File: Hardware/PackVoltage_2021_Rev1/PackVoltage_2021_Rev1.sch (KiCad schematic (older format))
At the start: 20 parts

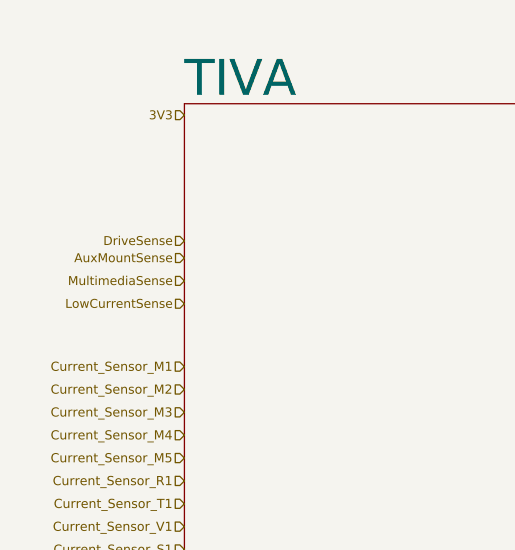
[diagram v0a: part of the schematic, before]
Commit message: Fixed anderson connections
Mistake made when rearranging busses so they would fit on sheet fixed
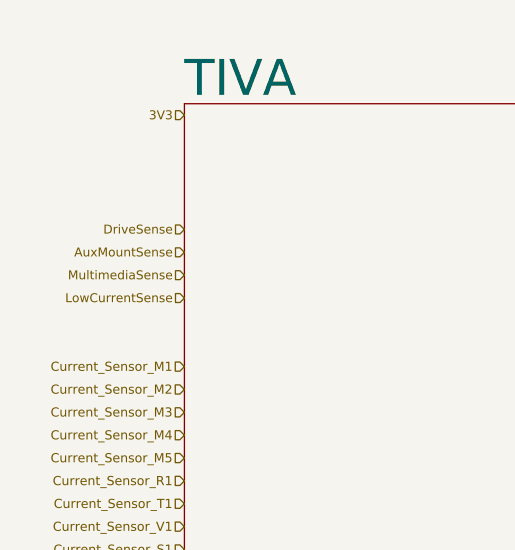
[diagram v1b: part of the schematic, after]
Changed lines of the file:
@@
 Pack Voltage Board
-$Sheet
-S 1200 850  2650 2100
-U 5F74F238
-F0 "TIVA" 157
-F1 "TIVA.sch" 157
-$EndSheet
 $Sheet
 S 1050 3550 2350 1550
@@
 Text Notes 5025 2600 2    79   ~ 0
 PV Tiva Pins
-Text HLabel 1200 1525 0    39   Input ~ 0
+Text HLabel 1200 1500 0    39   Input ~ 0
 AuxMountSense
-Text HLabel 1200 1625 0    39   Input ~ 0
+Text HLabel 1200 1600 0    39   Input ~ 0
 MultimediaSense
-Text HLabel 1200 1725 0    39   Input ~ 0
+Text HLabel 1200 1700 0    39   Input ~ 0
 LowCurrentSense
-Text HLabel 1200 1450 0    39   Input ~ 0
+Text HLabel 1200 1400 0    39   Input ~ 0
 DriveSense
 Wire Notes Line
@@
 	6075 1950 6200 1950
 NoConn ~ 6200 1550
+$Sheet
+S 1200 850  2650 2100
+U 5F74F238
+F0 "TIVA" 157
+F1 "TIVA.sch" 157
+$EndSheet
 $EndSCHEMATC

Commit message: updated busses, fuses, and some names
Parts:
- gave numbers to parts that had none: 1
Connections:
- net Anderson_M5 is gone; now on net Anderson_S1: Conn11.4 (PV+)
- net Anderson_S1: no longer Conn8.4 (PV+)
- new net Anderson_D1: Conn8.4 (PV+)
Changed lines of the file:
@@
 Driver_M3
 Text HLabel 1200 2800 0    40   Input ~ 0
-Current_Sensor_S1
+Current_Sensor_D1
 Text HLabel 1200 2600 0    40   Input ~ 0
 Current_Sensor_T1
@@
 Current_Sensor_V1
 Text HLabel 3850 2800 2    40   Output ~ 0
-Driver_S1
+Driver_D1
 Text HLabel 3850 2600 2    40   Output ~ 0
 Driver_T1
@@
 3V3
 Text HLabel 1050 6900 0    50   Input ~ 0
-Driver_S1
+Driver_D1
 Text HLabel 1050 6800 0    50   Input ~ 0
 Driver_T1
@@
 Current_Sensor_R1
 Text HLabel 3400 6900 2    50   Output ~ 0
-Current_Sensor_S1
+Current_Sensor_D1
 Text HLabel 3400 6800 2    50   Output ~ 0
 Current_Sensor_T1
@@
 Anderson_V1
 Text HLabel 8550 5750 2    50   Input ~ 0
-Anderson_S1
+Anderson_D1
 Text HLabel 3400 3600 2    50   Output ~ 0
 Anderson_M1
@@
 Anderson_V1
 Text HLabel 3400 6050 2    50   Output ~ 0
-Anderson_S1
+Anderson_D1
 Text HLabel 1050 3600 0    50   Input ~ 0
 PV
@@
 	9700 4600 9550 4600
 Text HLabel 9700 4600 2    50   Input ~ 0
-Anderson_M5
+Anderson_S1
 Text HLabel 1050 5050 0    50   Input ~ 0
-Driver_M5
+Driver_S1
 Text HLabel 3400 5050 2    50   Output ~ 0
-Current_Sensor_M5
+Current_Sensor_S1
 Text HLabel 3400 4000 2    50   Output ~ 0
-Anderson_M5
+Anderson_S1
 Text HLabel 1200 2400 0    40   Input ~ 0
-Current_Sensor_M5
+Current_Sensor_S1
 Text HLabel 3850 2400 2    40   Output ~ 0
-Driver_M5
+Driver_S1
 Text HLabel 6075 1850 0    50   Input ~ 0
 CameraCTL
@@
 Driver_A1
 $Comp
-L MRDT_Connectors:Molex_SL_10 Conn?
+L MRDT_Connectors:Molex_SL_10 Conn1
 U 1 1 5F87D729
 P 6400 2100
-F 0 "Conn?" H 6528 2658 60  0000 L CNN
+F 0 "Conn1" H 6528 2658 60  0000 L CNN
 F 1 "Molex_SL_10" H 6528 2552 60  0000 L CNN
 F 2 "" H 6400 2600 60  0001 C CNN

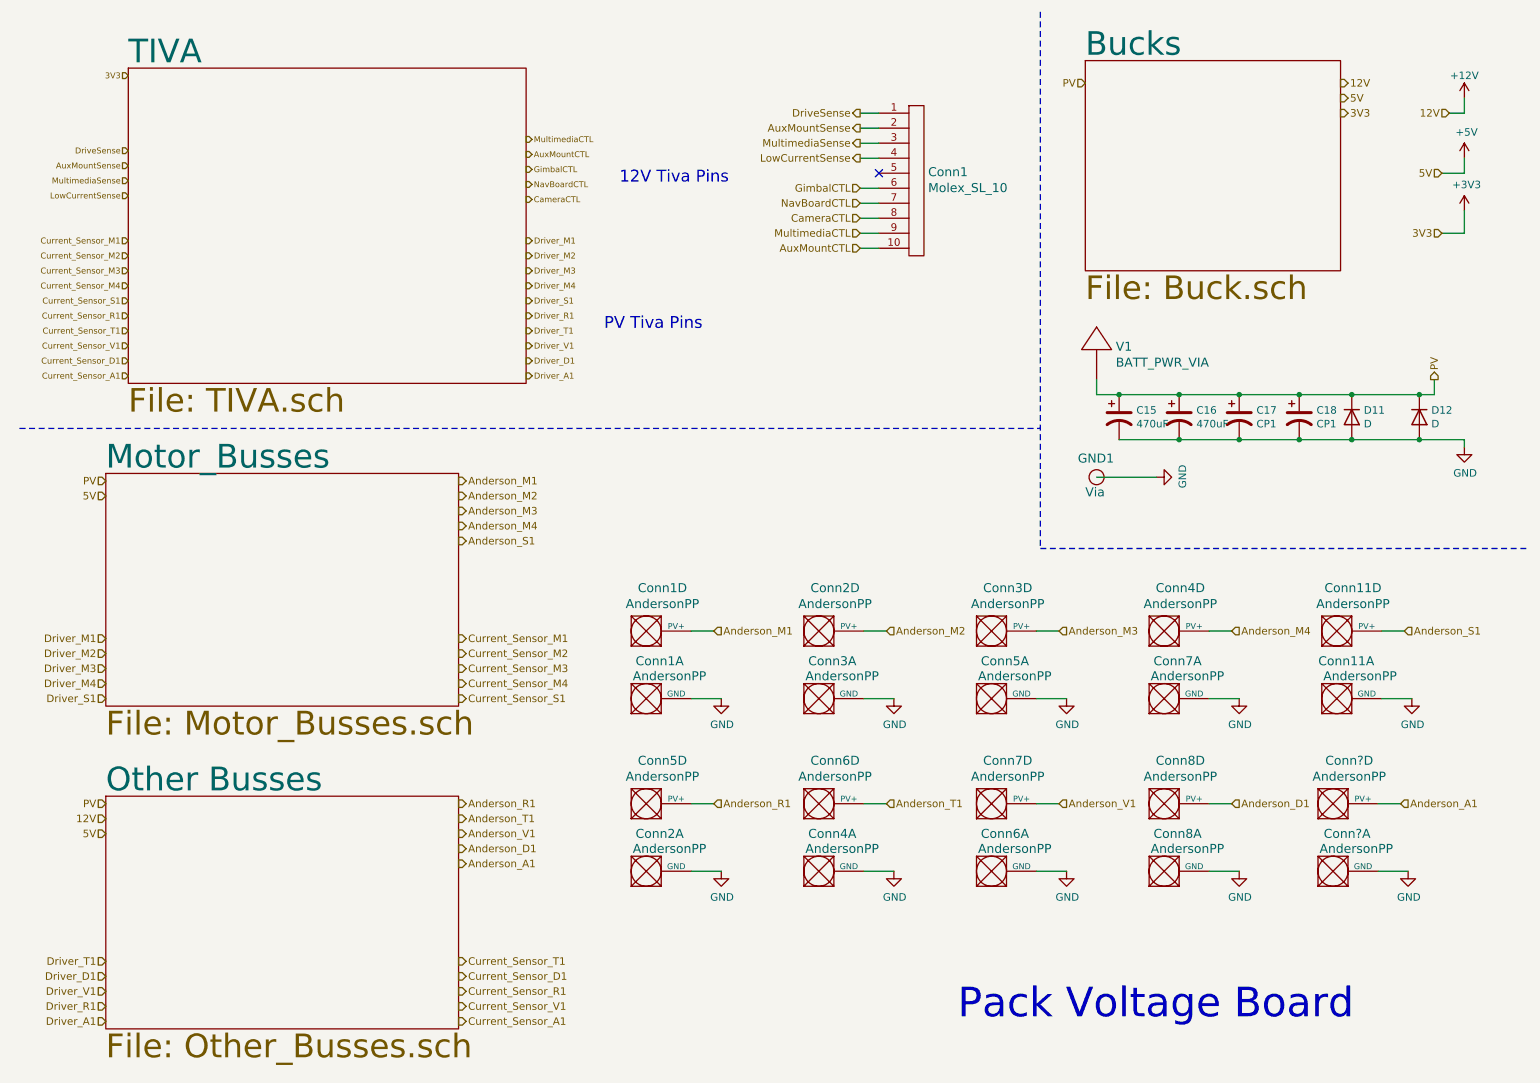
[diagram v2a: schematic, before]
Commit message: Fixed Hierarchial Pins/Labels
Removed Hierarchal labels from top sheet and replaced them with pins linked to the subsheets.
Renamed M5 Tiva pin to D1
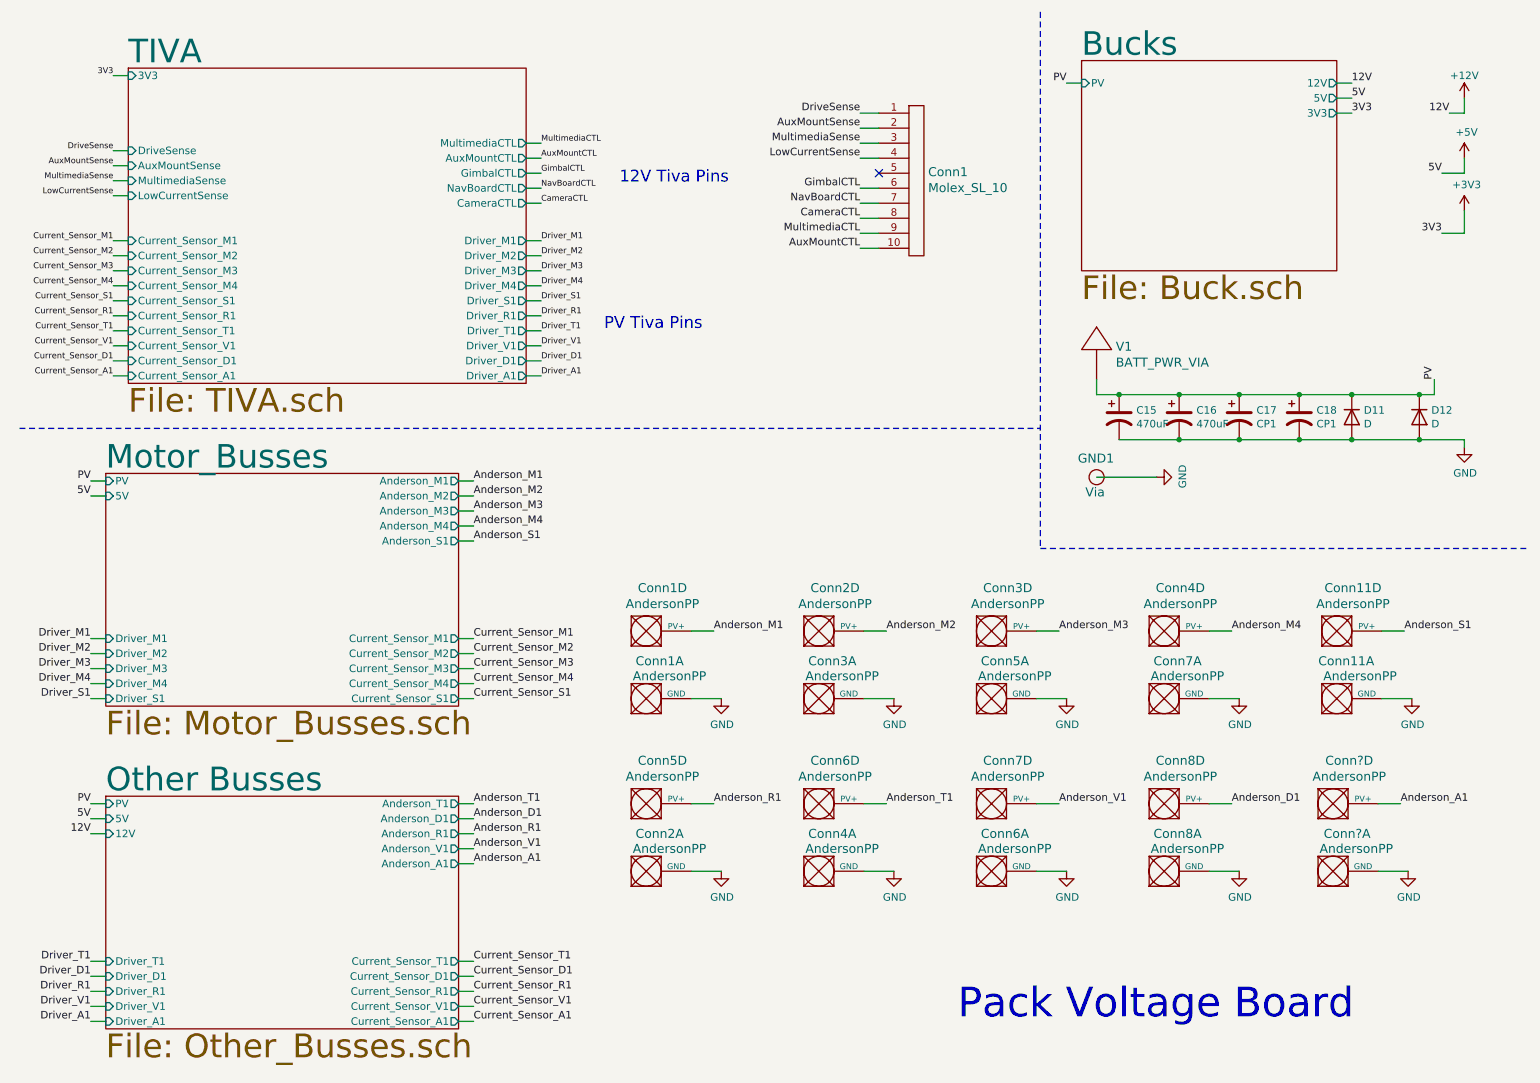
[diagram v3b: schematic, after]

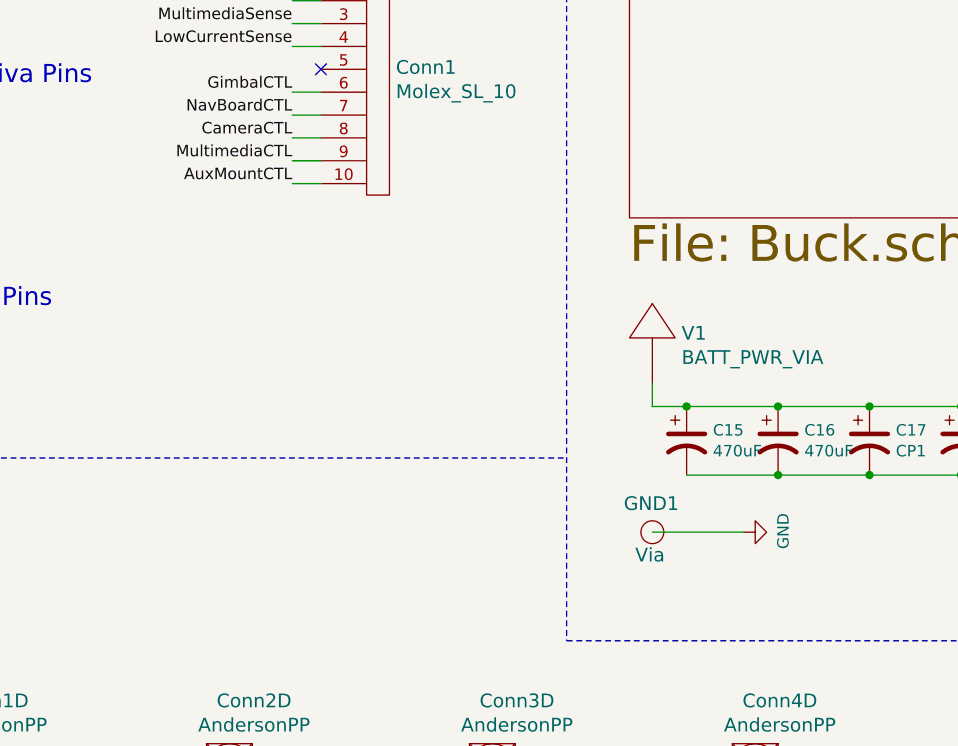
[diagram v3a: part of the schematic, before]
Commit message: corrected orientation of ground symbols, renamed buck converters, still need to update tiva with extra 12V pin
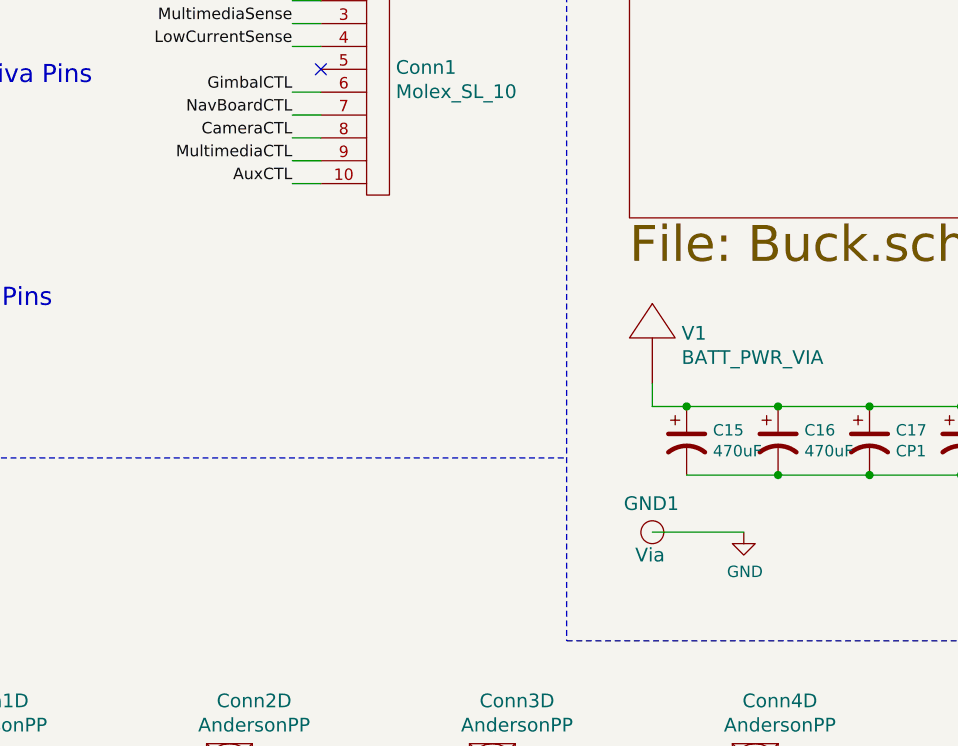
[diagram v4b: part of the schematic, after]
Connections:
- net AuxMountCTL: no longer Conn1.10
- new net AuxCTL: Conn1.10
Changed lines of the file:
@@
 F 3 "" H 8050 3575 50  0001 C CNN
 	1    8050 3575
-	0    -1   -1   0
+	1    0    0    -1
 $EndComp
 $Comp
@@
 MultimediaCTL
 Text Label 6075 2050 2    50   ~ 0
-AuxMountCTL
+AuxCTL
 Text Label 7450 950  2    50   ~ 0
 PV

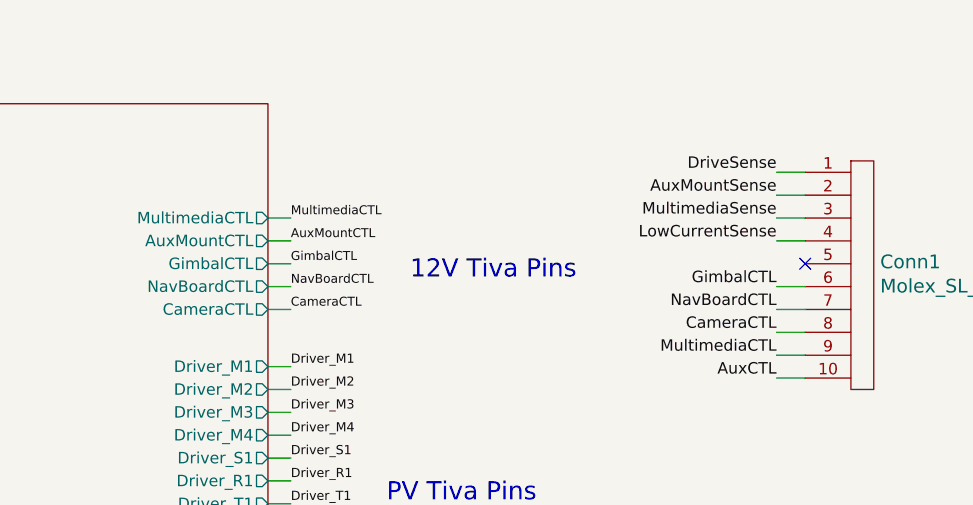
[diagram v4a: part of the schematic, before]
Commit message: Updated molex connector (Still need tiva pin)
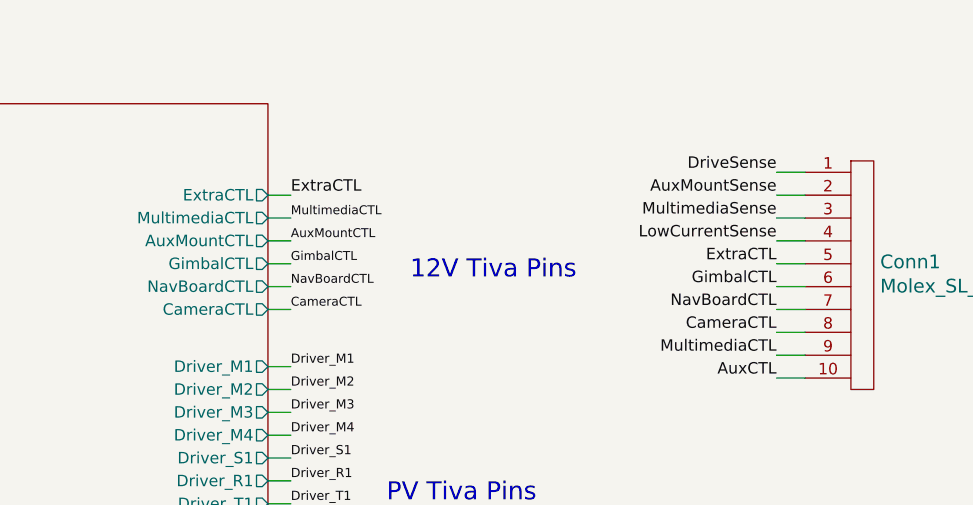
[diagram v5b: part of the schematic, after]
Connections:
- net ExtraCTL: now reaches Conn1.5
- no-connect marks 1 -> 0
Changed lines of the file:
@@
 Wire Wire Line
 	6075 1950 6200 1950
-NoConn ~ 6200 1550
-$Sheet
-S 1200 850  2650 2100
-U 5F74F238
-F0 "TIVA" 157
-F1 "TIVA.sch" 157
-F2 "Current_Sensor_R1" I L 1200 2500 50
-F3 "Driver_M1" O R 3850 2000 50
-F4 "Driver_M2" O R 3850 2100 50
-F5 "Driver_M3" O R 3850 2200 50
-F6 "Current_Sensor_S1" I L 1200 2400 50
-F7 "Current_Sensor_T1" I L 1200 2600 50
-F8 "Driver_M4" O R 3850 2300 50
-F9 "Driver_V1" O R 3850 2700 50
-F10 "Driver_R1" O R 3850 2500 50
-F11 "Current_Sensor_M1" I L 1200 2000 50
-F12 "Current_Sensor_M2" I L 1200 2100 50
-F13 "Current_Sensor_M3" I L 1200 2200 50
-F14 "Current_Sensor_M4" I L 1200 2300 50
-F15 "Current_Sensor_V1" I L 1200 2700 50
-F16 "Driver_S1" O R 3850 2400 50
-F17 "Driver_T1" O R 3850 2600 50
-F18 "3V3" I L 1200 900 50
-F19 "CameraCTL" O R 3850 1750 50
-F20 "NavBoardCTL" O R 3850 1650 50
-F21 "GimbalCTL" O R 3850 1550 50
-F22 "AuxMountSense" I L 1200 1500 50
-F23 "MultimediaSense" I L 1200 1600 50
-F24 "LowCurrentSense" I L 1200 1700 50
-F25 "DriveSense" I L 1200 1400 50
-F26 "AuxMountCTL" O R 3850 1450 50
-F27 "MultimediaCTL" O R 3850 1350 50
-F28 "Current_Sensor_A1" I L 1200 2900 50
-F29 "Driver_A1" O R 3850 2900 50
-F30 "Driver_D1" O R 3850 2800 50
-F31 "Current_Sensor_D1" I L 1200 2800 50
-$EndSheet
 Text Label 1100 1400 2    39   ~ 0
 DriveSense
@@
 3V3
 Wire Wire Line
-	3850 1350 3950 1350
-Wire Wire Line
-	3950 1450 3850 1450
-Wire Wire Line
-	3850 1550 3950 1550
-Wire Wire Line
-	3950 1650 3850 1650
-Wire Wire Line
-	3850 1750 3950 1750
-Wire Wire Line
 	3850 2000 3950 2000
 Wire Wire Line
@@
 Wire Wire Line
 	3950 2900 3850 2900
-Text Label 3950 1350 0    39   ~ 0
-MultimediaCTL
-Text Label 3950 1450 0    39   ~ 0
-AuxMountCTL
-Text Label 3950 1550 0    39   ~ 0
-GimbalCTL
-Text Label 3950 1650 0    39   ~ 0
-NavBoardCTL
-Text Label 3950 1750 0    39   ~ 0
-CameraCTL
 Text Label 3950 2000 0    40   ~ 0
 Driver_M1
@@
 	1    0    0    -1
 $EndComp
+Wire Wire Line
+	6075 1550 6200 1550
+Text Label 6075 1550 2    50   ~ 0
+ExtraCTL
+Text Label 3950 1750 0    39   ~ 0
+CameraCTL
+Text Label 3950 1650 0    39   ~ 0
+NavBoardCTL
+Text Label 3950 1550 0    39   ~ 0
+GimbalCTL
+Text Label 3950 1450 0    39   ~ 0
+AuxMountCTL
+Text Label 3950 1350 0    39   ~ 0
+MultimediaCTL
+Wire Wire Line
+	3850 1750 3950 1750
+Wire Wire Line
+	3950 1650 3850 1650
+Wire Wire Line
+	3850 1550 3950 1550
+Wire Wire Line
+	3950 1450 3850 1450
+Wire Wire Line
+	3850 1350 3950 1350
+Text Label 3950 1250 0    50   ~ 0
+ExtraCTL
+Wire Wire Line
+	3850 1250 3950 1250
+$Sheet
+S 1200 850  2650 2100
+U 5F74F238
+F0 "TIVA" 157
+F1 "TIVA.sch" 157
+F2 "Current_Sensor_R1" I L 1200 2500 50
+F3 "Driver_M1" O R 3850 2000 50
+F4 "Driver_M2" O R 3850 2100 50
+F5 "Driver_M3" O R 3850 2200 50
+F6 "Current_Sensor_S1" I L 1200 2400 50
+F7 "Current_Sensor_T1" I L 1200 2600 50
+F8 "Driver_M4" O R 3850 2300 50
+F9 "Driver_V1" O R 3850 2700 50
+F10 "Driver_R1" O R 3850 2500 50
+F11 "Current_Sensor_M1" I L 1200 2000 50
+F12 "Current_Sensor_M2" I L 1200 2100 50
+F13 "Current_Sensor_M3" I L 1200 2200 50
+F14 "Current_Sensor_M4" I L 1200 2300 50
+F15 "Current_Sensor_V1" I L 1200 2700 50
+F16 "Driver_S1" O R 3850 2400 50
+F17 "Driver_T1" O R 3850 2600 50
+F18 "3V3" I L 1200 900 50
+F19 "CameraCTL" O R 3850 1750 50
+F20 "NavBoardCTL" O R 3850 1650 50
+F21 "GimbalCTL" O R 3850 1550 50
+F22 "AuxMountSense" I L 1200 1500 50
+F23 "MultimediaSense" I L 1200 1600 50
+F24 "LowCurrentSense" I L 1200 1700 50
+F25 "DriveSense" I L 1200 1400 50
+F26 "AuxMountCTL" O R 3850 1450 50
+F27 "MultimediaCTL" O R 3850 1350 50
+F28 "Current_Sensor_A1" I L 1200 2900 50
+F29 "Driver_A1" O R 3850 2900 50
+F30 "Driver_D1" O R 3850 2800 50
+F31 "Current_Sensor_D1" I L 1200 2800 50
+F32 "ExtraCTL" O R 3850 1250 50
+$EndSheet
 $EndSCHEMATC

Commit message: Added GimbalSense, reannotated
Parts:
- removed Conn1: Molex_SL_10, symbol MRDT_Connectors:Molex_SL_10
- added Conn5: Molex_SL_05, symbol MRDT_Connectors:Molex_SL_05
- added Conn6: Molex_SL_07, symbol MRDT_Connectors:Molex_SL_07
- C3: renamed from C17; value CP1 -> 470uF
- C4: renamed from C18; value CP1 -> 470uF
- gave numbers to parts that had none: 1
- renumbered C15 to C1, C16 to C2, Conn8 to Conn10, Conn11 to Conn12, Conn5 to Conn2, Conn2 to Conn3, Conn6 to Conn4, Conn3 to Conn7, Conn5 to Conn7, Conn7 to Conn8, Conn6 to Conn8, Conn4 to Conn9, Conn7 to Conn9, D11 to D1, D12 to D2
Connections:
- net AuxCTL: now also Conn6.6
- net AuxMountSense: now also Conn5.2
- net CameraCTL: now also Conn6.4
- net DriveSense: now also Conn5.1
- net ExtraCTL: now also Conn6.1
- net GimbalCTL: now also Conn6.2
- net LowCurrentSense: now also Conn5.4
- net MultimediaCTL: now also Conn6.5
- net MultimediaSense: now also Conn5.3
- net NavBoardCTL: now also Conn6.3
- new net GimbalSense: Conn5.5
- no-connect marks 0 -> 1

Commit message: updated footprints
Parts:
- C1, C2, C3, C4: footprint (none) -> Capacitor_SMD:C_0603_1608Metric_Pad1.05x0.95mm_HandSolder
- Conn1, Conn10, Conn11, Conn12, Conn2, Conn3, Conn4, Conn7, Conn8, Conn9: footprint (none) -> MRDT_Connectors:Anderson_2_Horizontal_Side_by_Side; symbol MRDT_Connectors:AndersonPP -> PackVoltage_2021_Rev1-rescue:AndersonPP-MRDT_Connectors
- Conn5: footprint (none) -> MRDT_Connectors:MOLEX_SL_05_Horizontal; symbol MRDT_Connectors:Molex_SL_05 -> PackVoltage_2021_Rev1-rescue:Molex_SL_05-MRDT_Connectors
- Conn6: footprint (none) -> MRDT_Connectors:MOLEX_SL_07_Horizontal; symbol MRDT_Connectors:Molex_SL_07 -> PackVoltage_2021_Rev1-rescue:Molex_SL_07-MRDT_Connectors
- D1, D2: footprint (none) -> Diode_SMD:D_0201_0603Metric
- GND1: footprint (none) -> MRDT_Drill_Holes:BATT_PWR_VIA; symbol MRDT_Drill_Holes:Via -> PackVoltage_2021_Rev1-rescue:Via-MRDT_Drill_Holes
- V1: footprint (none) -> MRDT_Drill_Holes:BATT_PWR_VIA; symbol MRDT_Drill_Holes:BATT_PWR_VIA -> PackVoltage_2021_Rev1-rescue:BATT_PWR_VIA-MRDT_Drill_Holes
